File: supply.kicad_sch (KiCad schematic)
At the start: 165 parts, among them J10001 JST_SH_1x4_BM04B-SRSS-TB-LF-SN, J1001 BarrelJack_3167288, Q10001 BSS138PW, Q10002 SI7613DN-T1-GE3, Q1001 SI7613DN-T1-GE3, Q1002 BSS138PW, Q20001 BSS138PW, SW1001 SW_CVS-02B, SW1002 SW_KMR211NGLFS_SMD, U10001 NCP718BSN330T1G, U10002 MPM54304GMN, U10003 MPM54304GMN, U10004 MAX16150A_SOT, U10005 LTC4412IS6, U10006 LM3880, U10007 MP8869S, U10008 XC6230H001ER-G, U10009 MAX812REUS+T, U1001 LTC4412IS6, U10010 PAC1954T-E_VQFN, U10011 PAC1954T-E_VQFN

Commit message: Sync new components with PCB
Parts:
- removed SW?: SW_CVS-02B, antmicro-footprints:SW_DIP_SPSTx02_Slide_Copal_CVS-02xB_W5.9mm_P1mm, symbol antmicroSlideSwitches:SW_CVS-02B
- removed T?: TestPoint_Probe_1206_RCW-0C, sodimm-ddr5-tester-footprints:PROBE_PAD_1206, symbol sodimm-ddr5-tester:TestPoint_Probe_1206_RCW-0C
- added SW10002: CVS-03B, antmicro-footprints:SW_DIP_SPSTx03_Slide_Copal_CVS-03xB_W5.9mm_P1mm, symbol antmicroSlideSwitches:CVS-03B
- added TP10001: TP_1206_SMD_RCW-0C, antmicro-footprints:TP_1206_SMD_RCW-0C, symbol antmicroTestPoints:TP_1206_SMD_RCW-0C
- gave numbers to parts that had none: 24
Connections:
- net GND: now also SW10002.4, SW10002.7
- net PWR_SCL: now also SW10002.1, SW10002.2
- net QDCDC1_SCL: now also SW10002.6
- net QDCDC2_SCL: now also SW10002.5
- net at NT10002.2, R10012.2: now also TP10001.1
- new net FTDI_DIS: SW10002.3

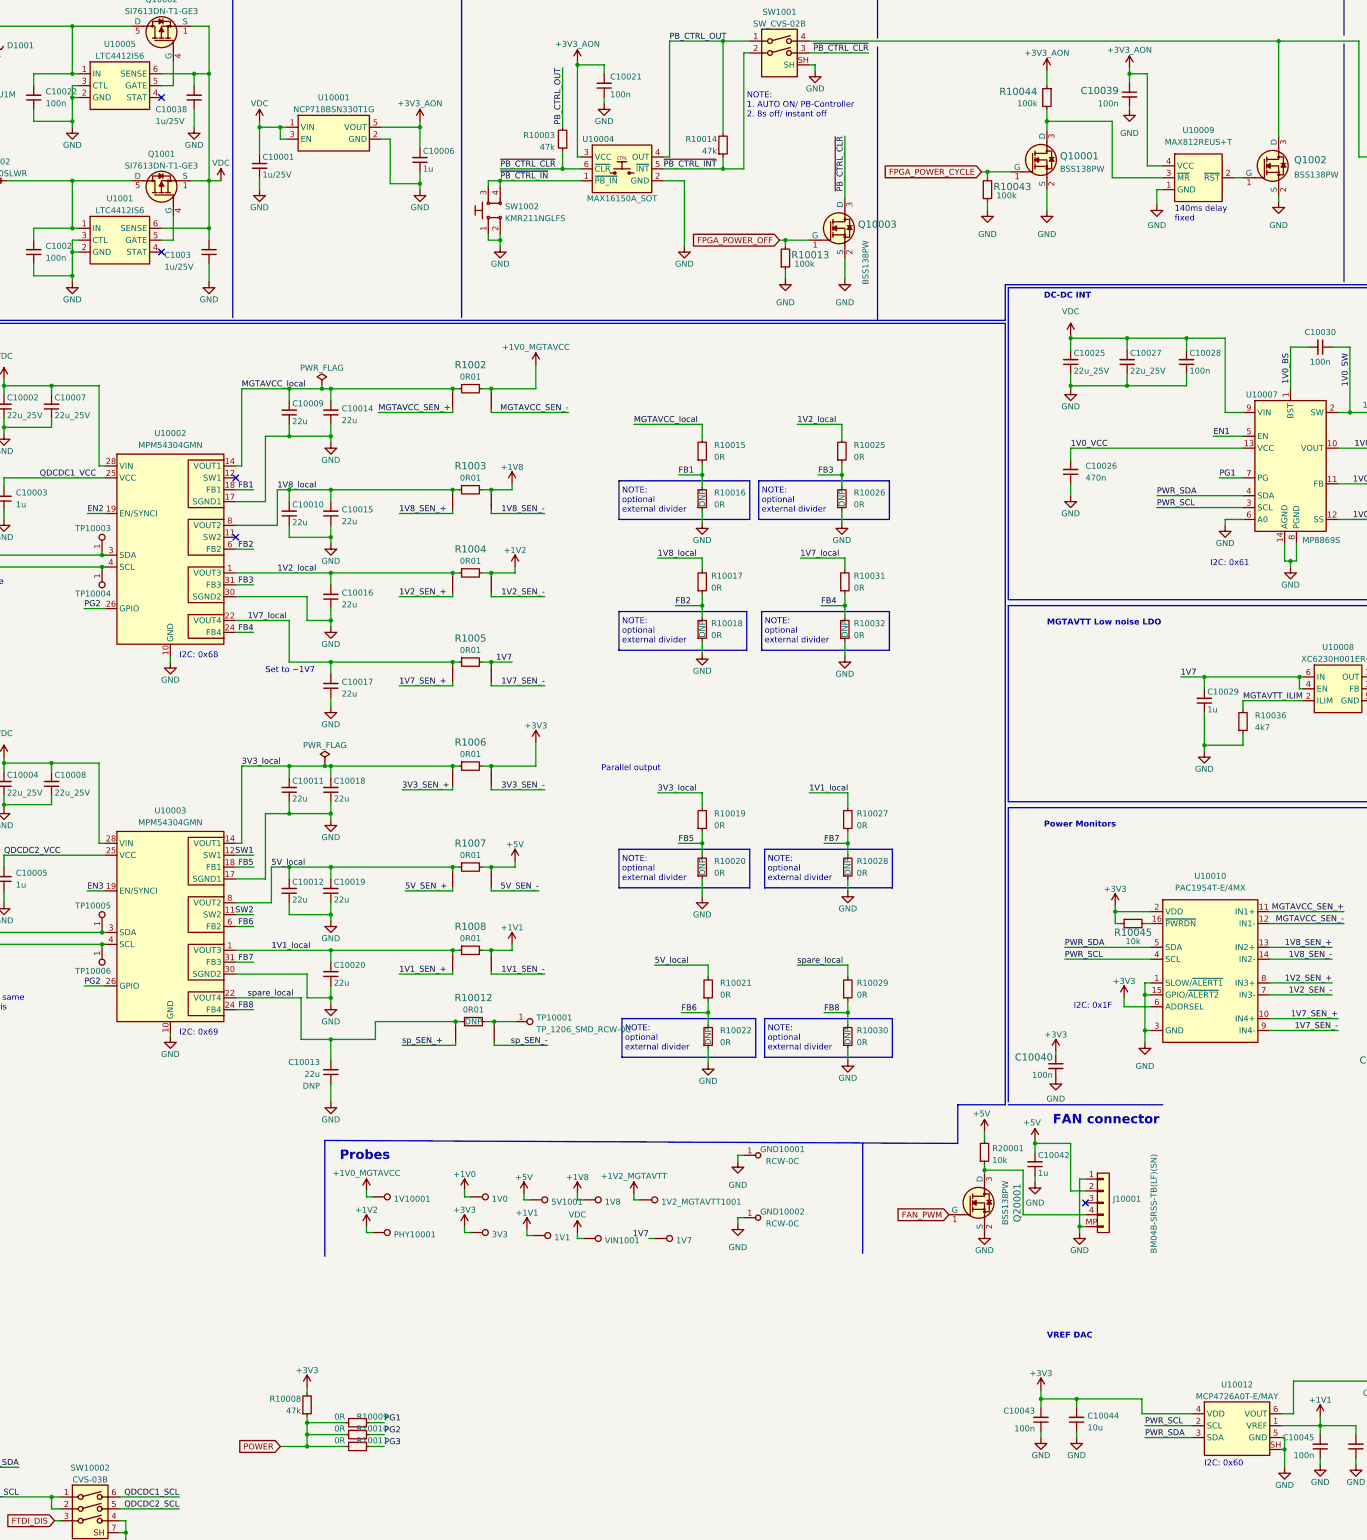
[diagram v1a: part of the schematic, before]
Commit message: Continue optimizing placement and layout of misc. circuitry
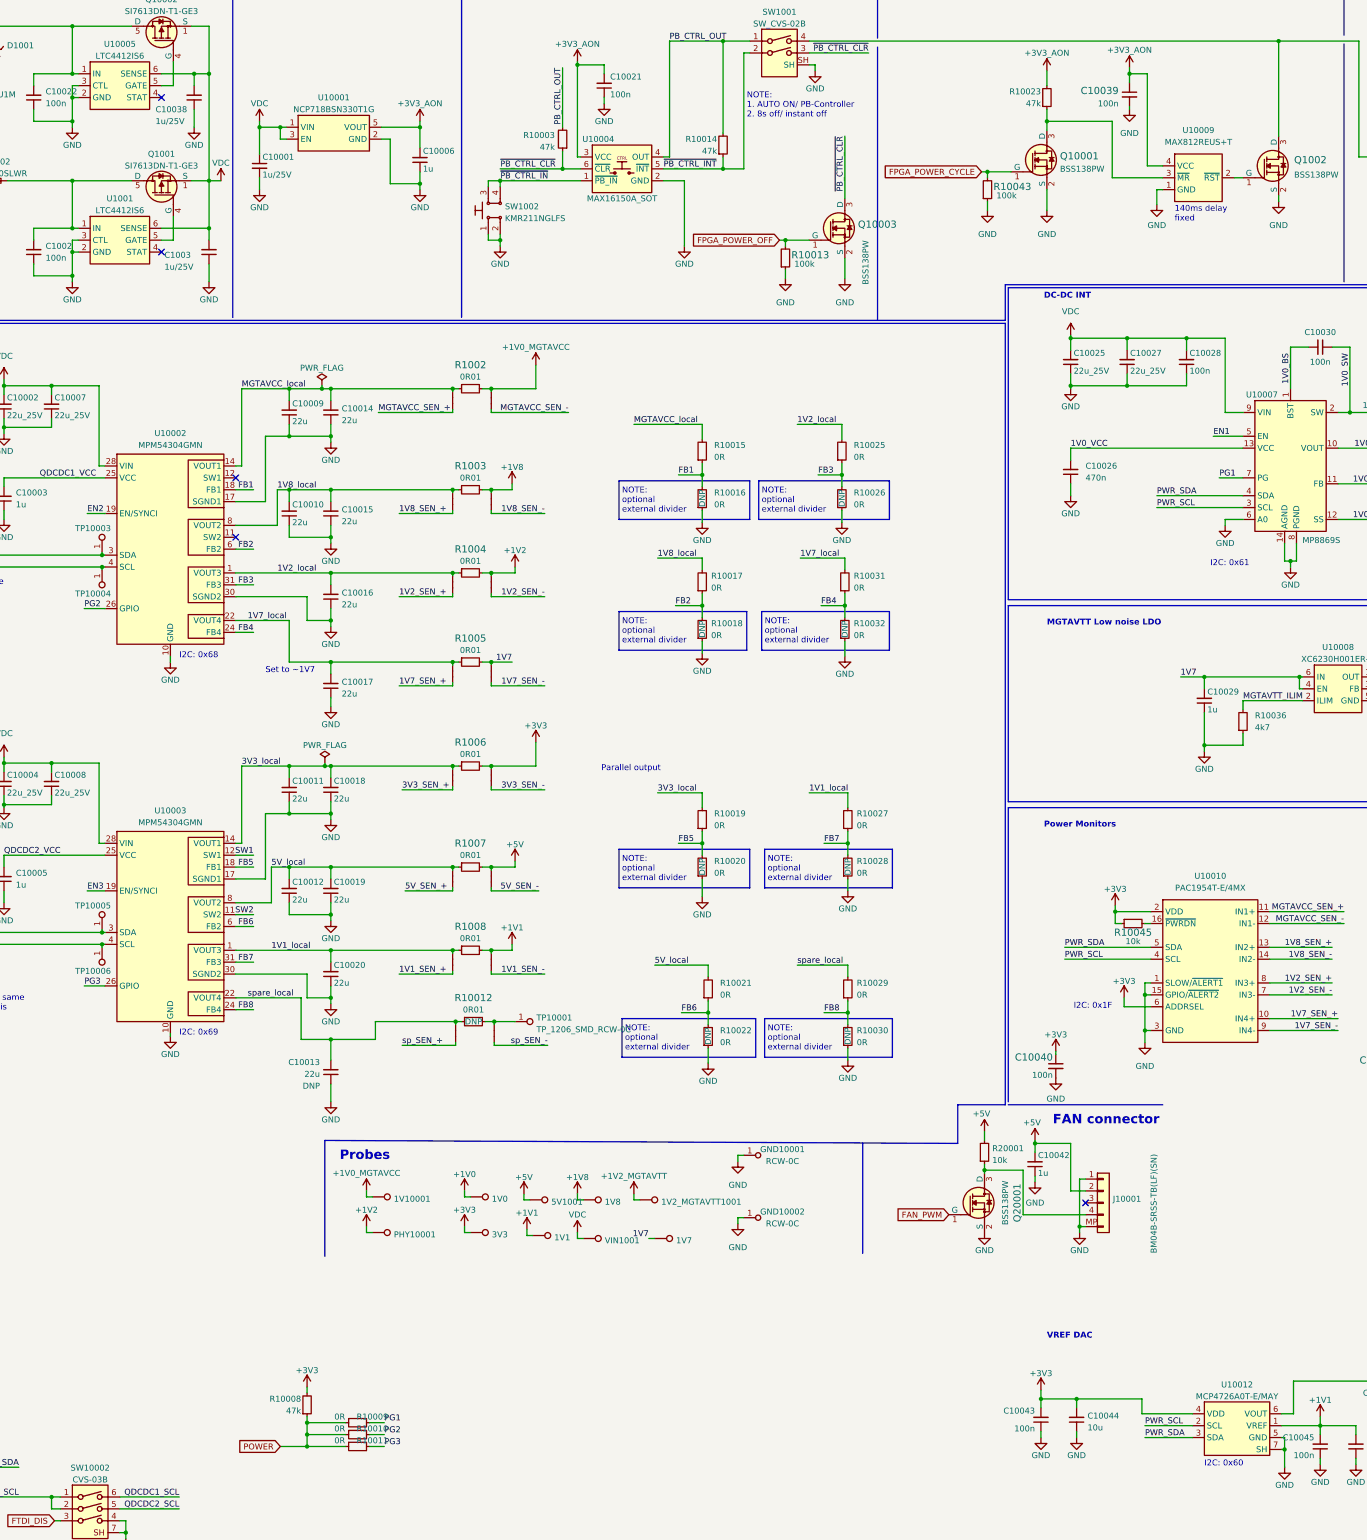
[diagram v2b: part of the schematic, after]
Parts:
- removed R10044: R_100k_0402, sodimm-ddr5-tester-footprints:R_0402_1005Metric, symbol sodimm-ddr5-tester:R_100k_0402
- added R10023: R_47k_0402, sodimm-ddr5-tester-footprints:R_0402_1005Metric, symbol sodimm-ddr5-tester:R_47k_0402
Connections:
- net +3V3_AON: now also R10023.2
- net GND: now also U10012.7 (SH); no longer U10012.SH
- net PG2: no longer U10003.26 (GPIO)
- net PG3: now also U10003.26 (GPIO)
- net at Q10001.3 (D), U10009.3 (~{MR}): now also R10023.1
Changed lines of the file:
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@@
     (effects (font (size 1.27 1.27)) (justify left bottom))
   )
-  (label "PG2" (at 69.215 227.33 0)
+  (label "PG3" (at 69.215 227.33 0)
     (effects (font (size 1.27 1.27)) (justify left bottom))
   )
@@
     (pin "1")
   )
+  (symbol (lib_name "MCP4726A0T-E_MAY_1") (lib_id "antmicroDataAcquisitionDigitaltoAnalogConvertersDAC:MCP4726A0T-E_MAY") (at 306.07 318.77 0) (unit 1)
+    (in_bom yes) (on_board yes) (fields_autoplaced)
+    (property "Reference" "U10012" (id 0) (at 315.595 312.545 0)
+      (effects (font (size 1.27 1.27) (thickness 0.15)))
+    )
+    (property "Value" "MCP4726A0T-E_MAY" (id 1) (at 339.09 328.93 0)
+      (effects (font (size 1.27 1.27) (thickness 0.15)) (justify left bottom) hide)
+    )
+    (property "Footprint" "antmicro-footprints:DFN-6-1EP_2x2mm_P0.65mm_EP1x1.6mm" (id 2) (at 339.09 331.47 0)
+      (effects (font (size 1.27 1.27) (thickness 0.15)) (justify left bottom) hide)
+    )
+    (property "Datasheet" "https://ww1.microchip.com/downloads/en/DeviceDoc/22272C.pdf" (id 3) (at 339.09 334.01 0)
+      (effects (font (size 1.27 1.27) (thickness 0.15)) (justify left bottom) hide)
+    )
+    (property "Manufacturer" "Microchip Technology" (id 4) (at 339.09 323.85 0)
+      (effects (font (size 1.27 1.27) (thickness 0.15)) (justify left bottom) hide)
+    )
+    (property "MPN" "MCP4726A0T-E/MAY" (id 5) (at 315.595 315.0687 0)
+      (effects (font (size 1.27 1.27) (thickness 0.15)))
+    )
+    (property "Author" "Antmicro" (id 6) (at 339.09 336.55 0)
+      (effects (font (size 1.27 1.27) (thickness 0.15)) (justify left bottom) hide)
+    )
+    (property "License" "Apache-2.0" (id 7) (at 339.09 339.09 0)
+      (effects (font (size 1.27 1.27) (thickness 0.15)) (justify left bottom) hide)
+    )
+    (pin "1")
+    (pin "2")
+    (pin "3")
+    (pin "4")
+    (pin "5")
+    (pin "6")
+    (pin "7")
+  )
   (symbol (lib_id "sodimm-ddr5-tester:GND") (at 34.29 66.675 0) (unit 1)
     (in_bom yes) (on_board yes) (fields_autoplaced)
@@
     (pin "1")
   )
+  (symbol (lib_id "sodimm-ddr5-tester:R_47k_0402") (at 274.955 40.005 90) (unit 1)
+    (in_bom yes) (on_board yes)
+    (property "Reference" "R10023" (id 0) (at 273.685 36.195 90)
+      (effects (font (size 1.27 1.27)) (justify left))
+    )
+    (property "Value" "R_47k_0402" (id 1) (at 287.655 19.685 0)
+      (effects (font (size 1.27 1.27) (thickness 0.15)) (justify left bottom) hide)
+    )
+    (property "Footprint" "sodimm-ddr5-tester-footprints:R_0402_1005Metric" (id 2) (at 290.195 19.685 0)
+      (effects (font (size 1.27 1.27) (thickness 0.15)) (justify left bottom) hide)
+    )
+    (property "Datasheet" "https://www.bourns.com/docs/product-datasheets/cr.pdf" (id 3) (at 292.735 19.685 0)
+      (effects (font (size 1.27 1.27) (thickness 0.15)) (justify left bottom) hide)
+    )
+    (property "Manufacturer" "Bourns" (id 4) (at 297.815 19.685 0)
+      (effects (font (size 1.27 1.27) (thickness 0.15)) (justify left bottom) hide)
+    )
+    (property "MPN" "CR0402-FX-4702GLF" (id 5) (at 295.275 19.685 0)
+      (effects (font (size 1.27 1.27) (thickness 0.15)) (justify left bottom) hide)
+    )
+    (property "Val" "47k" (id 6) (at 273.685 38.735 90)
+      (effects (font (size 1.27 1.27) (thickness 0.15)) (justify left))
+    )
+    (property "License" "Apache-2.0" (id 7) (at 300.355 19.685 0)
+      (effects (font (size 1.27 1.27) (thickness 0.15)) (justify left bottom) hide)
+    )
+    (property "Author" "Antmicro" (id 8) (at 302.895 19.685 0)
+      (effects (font (size 1.27 1.27) (thickness 0.15)) (justify left bottom) hide)
+    )
+    (property "Tolerance" "1%" (id 9) (at 285.115 19.685 0)
+      (effects (font (size 1.27 1.27)) (justify left bottom) hide)
+    )
+    (pin "1")
+    (pin "2")
+  )
   (symbol (lib_id "sodimm-ddr5-tester:GND") (at 180.34 38.735 0) (unit 1)
     (in_bom yes) (on_board yes)
@@
     (pin "1")
   )
-  (symbol (lib_id "sodimm-ddr5-tester:R_100k_0402") (at 274.955 34.925 270) (unit 1)
-    (in_bom yes) (on_board yes)
-    (property "Reference" "R10044" (id 0) (at 264.795 36.195 90)
-      (effects (font (size 1.524 1.524)) (justify left))
-    )
-    (property "Value" "R_100k_0402" (id 1) (at 262.255 55.245 0)
-      (effects (font (size 1.27 1.27) (thickness 0.15)) (justify left bottom) hide)
-    )
-    (property "Footprint" "sodimm-ddr5-tester-footprints:R_0402_1005Metric" (id 2) (at 259.715 55.245 0)
-      (effects (font (size 1.27 1.27) (thickness 0.15)) (justify left bottom) hide)
-    )
-    (property "Datasheet" "https://www.bourns.com/docs/product-datasheets/cr.pdf" (id 3) (at 257.175 55.245 0)
-      (effects (font (size 1.27 1.27) (thickness 0.15)) (justify left bottom) hide)
-    )
-    (property "Manufacturer" "Bourns" (id 4) (at 252.095 55.245 0)
-      (effects (font (size 1.27 1.27) (thickness 0.15)) (justify left bottom) hide)
-    )
-    (property "MPN" "CR0402-FX-1003GLF" (id 5) (at 254.635 55.245 0)
-      (effects (font (size 1.27 1.27) (thickness 0.15)) (justify left bottom) hide)
-    )
-    (property "Val" "100k" (id 6) (at 268.605 38.735 90)
-      (effects (font (size 1.27 1.27) (thickness 0.15)) (justify left))
-    )
-    (property "License" "Apache-2.0" (id 7) (at 249.555 55.245 0)
-      (effects (font (size 1.27 1.27) (thickness 0.15)) (justify left bottom) hide)
-    )
-    (property "Author" "Antmicro" (id 8) (at 247.015 55.245 0)
-      (effects (font (size 1.27 1.27) (thickness 0.15)) (justify left bottom) hide)
-    )
-    (property "Tolerance" "1%" (id 9) (at 264.795 55.245 0)
-      (effects (font (size 1.27 1.27)) (justify left bottom) hide)
-    )
-    (pin "1")
-    (pin "2")
-  )
   (symbol (lib_id "sodimm-ddr5-tester:GND") (at 295.91 239.395 0) (unit 1)
     (in_bom yes) (on_board yes) (fields_autoplaced)
@@
     (pin "1")
   )
-  (symbol (lib_id "antmicroDataAcquisitionDigitaltoAnalogConvertersDAC:MCP4726A0T-E_MAY") (at 306.07 318.77 0) (unit 1)
-    (in_bom yes) (on_board yes) (fields_autoplaced)
-    (property "Reference" "U10012" (id 0) (at 315.595 312.545 0)
-      (effects (font (size 1.27 1.27) (thickness 0.15)))
-    )
-    (property "Value" "MCP4726A0T-E_MAY" (id 1) (at 339.09 328.93 0)
-      (effects (font (size 1.27 1.27) (thickness 0.15)) (justify left bottom) hide)
-    )
-    (property "Footprint" "antmicro-footprints:DFN-6-1EP_2x2mm_P0.65mm_EP1x1.6mm" (id 2) (at 339.09 331.47 0)
-      (effects (font (size 1.27 1.27) (thickness 0.15)) (justify left bottom) hide)
-    )
-    (property "Datasheet" "https://ww1.microchip.com/downloads/en/DeviceDoc/22272C.pdf" (id 3) (at 339.09 334.01 0)
-      (effects (font (size 1.27 1.27) (thickness 0.15)) (justify left bottom) hide)
-    )
-    (property "Manufacturer" "Microchip Technology" (id 4) (at 339.09 323.85 0)
-      (effects (font (size 1.27 1.27) (thickness 0.15)) (justify left bottom) hide)
-    )
-    (property "MPN" "MCP4726A0T-E/MAY" (id 5) (at 315.595 315.0687 0)
-      (effects (font (size 1.27 1.27) (thickness 0.15)))
-    )
-    (property "Author" "Antmicro" (id 6) (at 339.09 336.55 0)
-      (effects (font (size 1.27 1.27) (thickness 0.15)) (justify left bottom) hide)
-    )
-    (property "License" "Apache-2.0" (id 7) (at 339.09 339.09 0)
-      (effects (font (size 1.27 1.27) (thickness 0.15)) (justify left bottom) hide)
-    )
-    (pin "1")
-    (pin "2")
-    (pin "3")
-    (pin "4")
-    (pin "5")
-    (pin "6")
-    (pin "SH")
-  )
   (symbol (lib_id "sodimm-ddr5-tester:GND") (at 231.775 76.2 0) (unit 1)
